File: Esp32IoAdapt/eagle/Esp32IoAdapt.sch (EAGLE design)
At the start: 9 parts

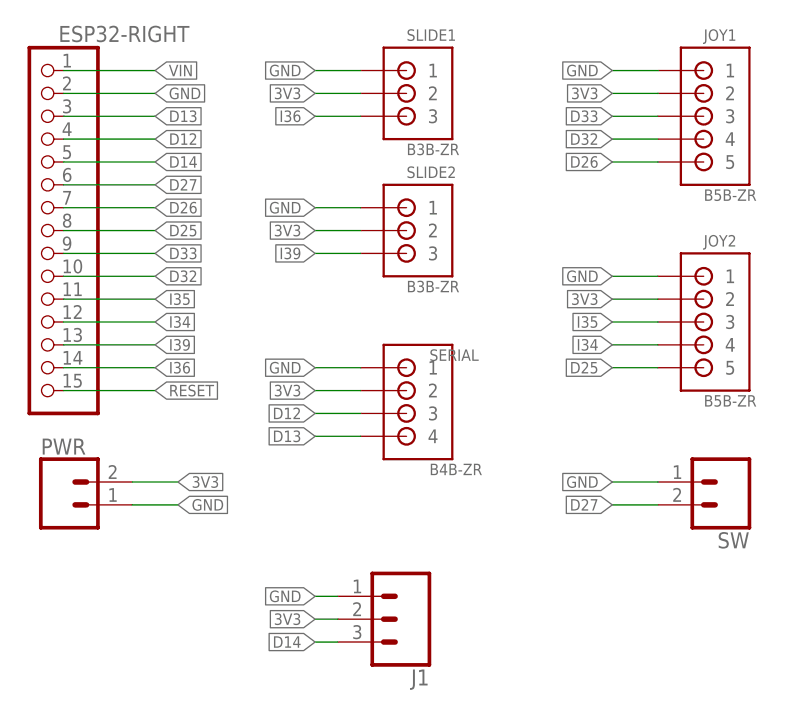
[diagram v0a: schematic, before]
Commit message: Renamed connectors
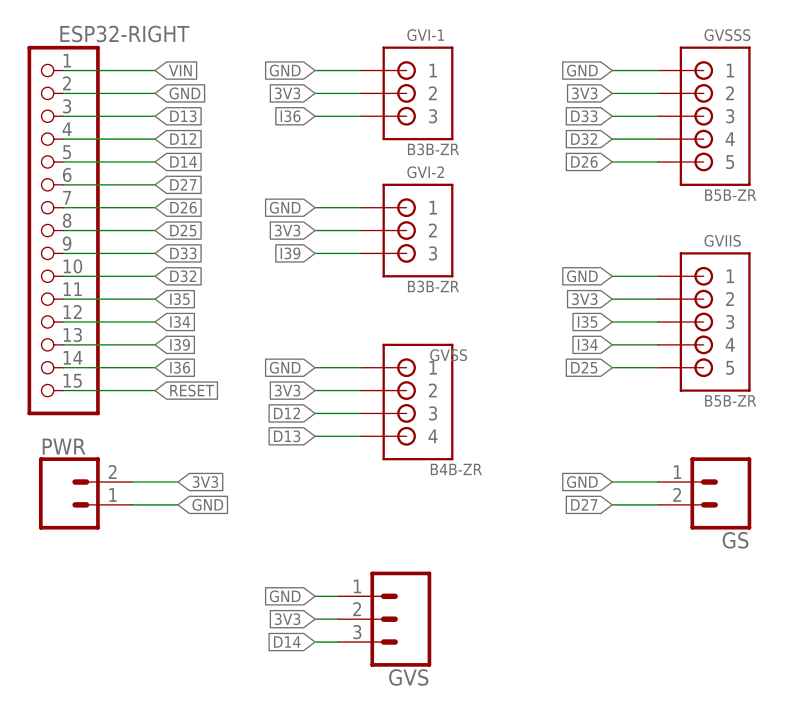
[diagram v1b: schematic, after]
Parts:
- renumbered J1 to GVS, JOY1 to GVSSS, JOY2 to GVIIS, SERIAL to GVSS, SLIDE1 to GVI-1, SLIDE2 to GVI-2, SW to GS

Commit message: Adjusted labels
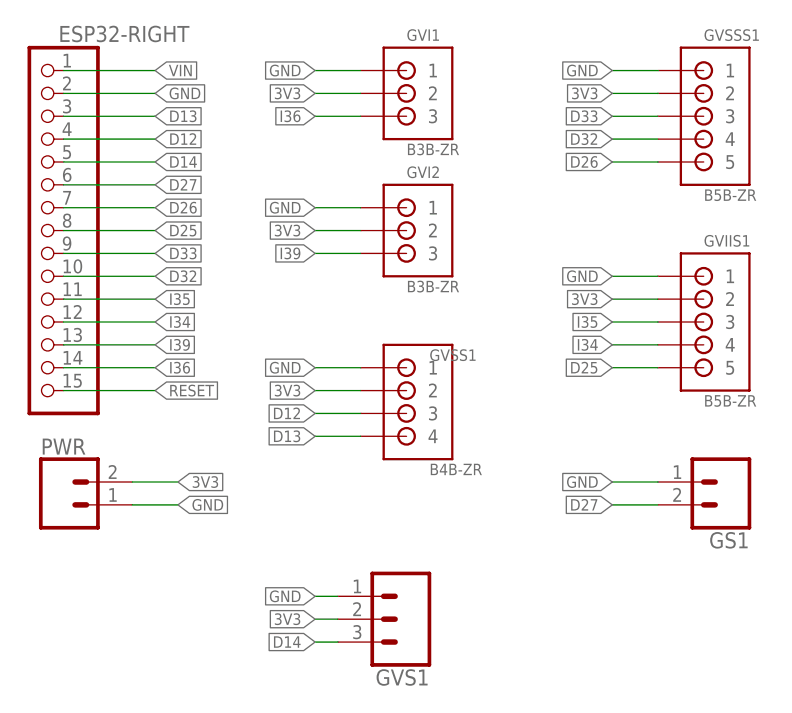
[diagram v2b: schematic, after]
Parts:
- renumbered GS to GS1, GVI-1 to GVI1, GVI-2 to GVI2, GVIIS to GVIIS1, GVS to GVS1, GVSS to GVSS1, GVSSS to GVSSS1

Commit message: More connector labelling
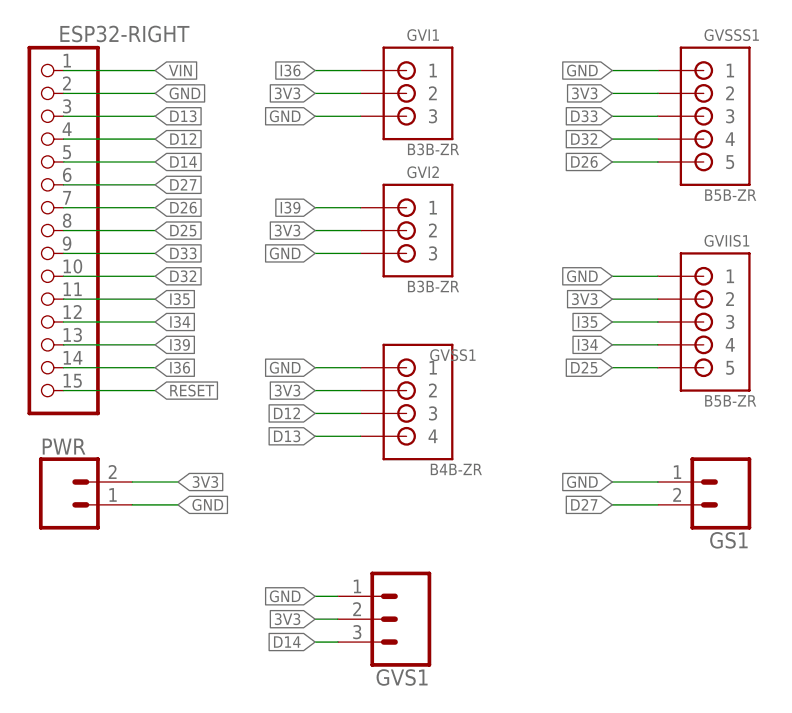
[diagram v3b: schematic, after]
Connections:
- net GND: now also GVI1.3, GVI2.3; no longer GVI1.1, GVI2.1
- net I36: now also GVI1.1; no longer GVI1.3
- net I39: now also GVI2.1; no longer GVI2.3
